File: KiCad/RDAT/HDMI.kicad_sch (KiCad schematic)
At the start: 37 parts, among them J3 HDMI_A, Q4 2N7002, Q5 2SK3018, Q6 2SK3018, Q7 2SK3018, U13 TPAZ1023-04F, U14 TPAZ1023-04F

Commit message: Added Libs and DOCS
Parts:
- J3: footprint A_HDJ_Library:HDMI_A_Molex_208658-1001_Horizontal -> footprints:AMPHENOL_MHDRA111M0; JLCPCB_LINK (none) -> https://www.digikey.com/en/products/detail/amphenol-cs-comm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
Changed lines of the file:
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@@
 			)
 		)
-		(property "Footprint" "A_HDJ_Library:HDMI_A_Molex_208658-1001_Horizontal"
+		(property "Footprint" "footprints:AMPHENOL_MHDRA111M0"
 			(at 179.705 72.39 0)
 			(effects
@@
 			)
 		)
-		(property "Datasheet" "https://en.wikipedia.org/wiki/HDMI"
+		(property "Datasheet" "https://cdn.amphenol-cs.com/media/wysiwyg/files/drawing/mhdra111xx.pdf"
 			(at 179.705 72.39 0)
 			(effects
@@
 			)
 		)
-		(property "JLCPCB_LINK" ""
+		(property "JLCPCB_LINK" "https://www.digikey.com/en/products/detail/amphenol-cs-commercial-products/MHDRA111M0/8572891"
 			(at 179.07 72.39 0)
 			(effects
@@
 					(size 1.27 1.27)
 				)
+				(hide yes)
 			)
 		)

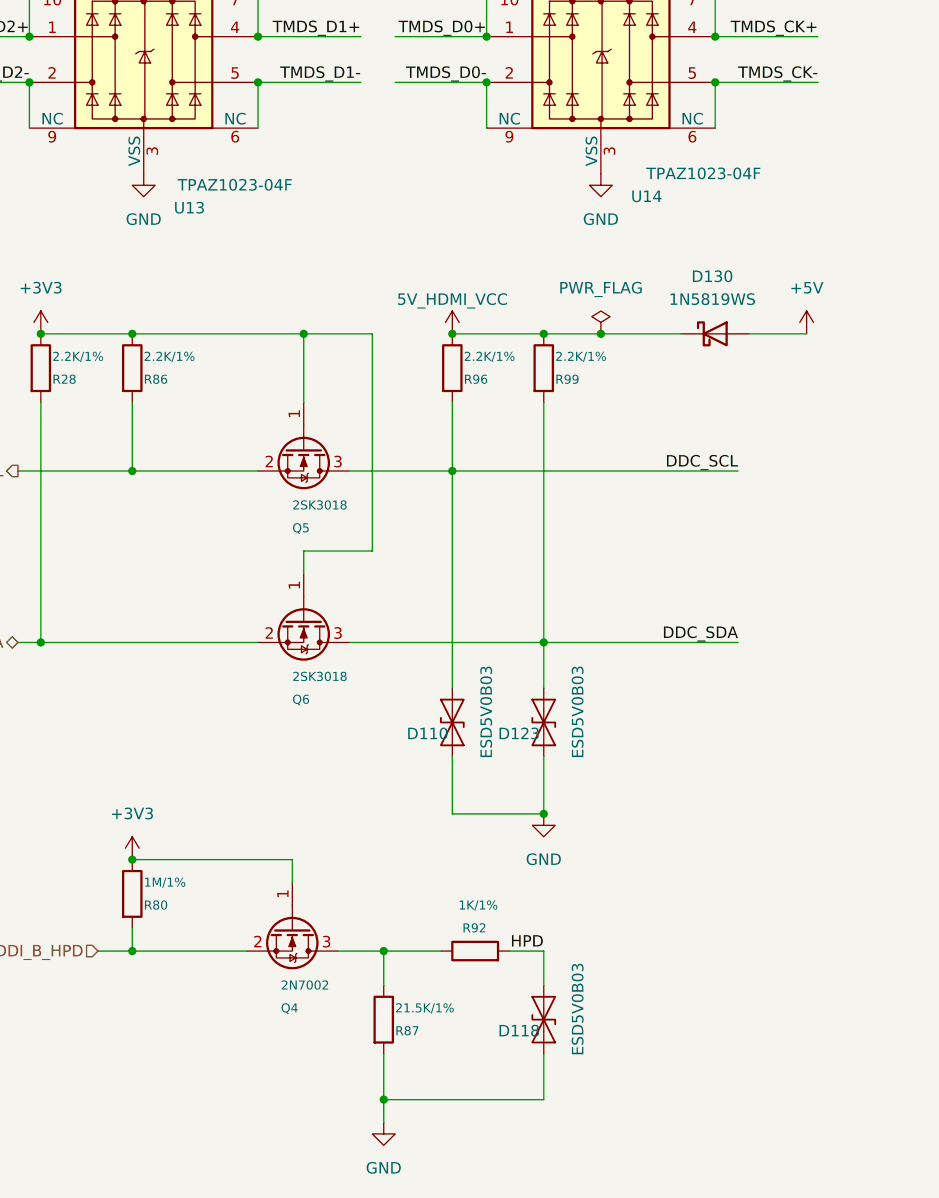
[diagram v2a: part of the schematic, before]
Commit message: Sourced and documented all parts
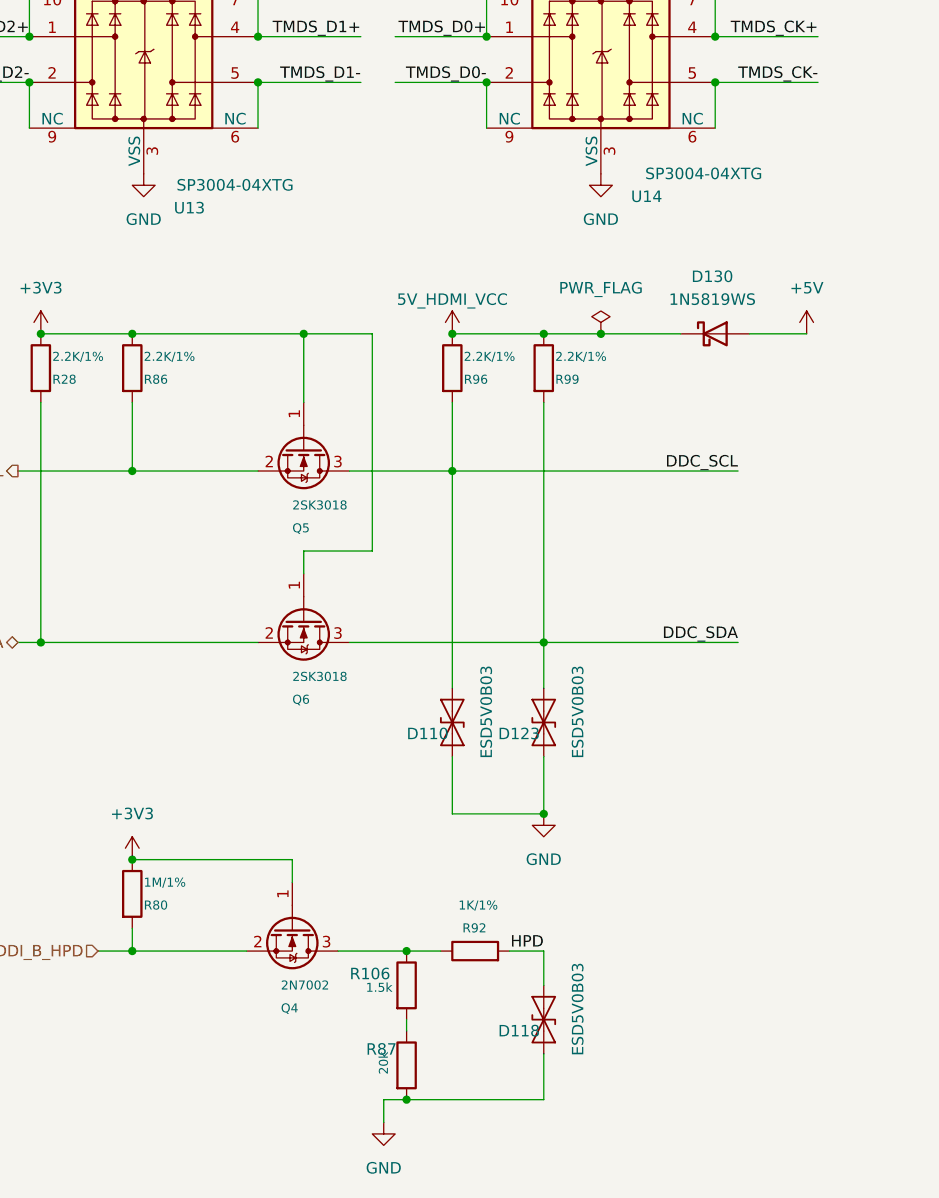
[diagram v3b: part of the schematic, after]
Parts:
- added R106: 1.5k, A_HDJ_Library:R_0402_1005Metric, symbol Device:R
- C25, C26, C27, C28, C29, C30, C31, C91, C92: JLCPCB_LINK (none) -> https://jlcpcb.com/partdetail/291005-CL05B104KB54PNC/C307331
- D110, D118, D123: footprint A_HDJ_Library:D_0402_1005Metric -> Diode_SMD:D_SOD-882; JLCPCB_LINK (none) -> https://jlcpcb.com/partdetail/TechPublic-ESD5V0B031006/C521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
- D130: JLCPCB_LINK (none) -> https://jlcpcb.com/partdetail/GuangdongHottech-1N5819WS/C19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
- F1: JLCPCB_LINK (none) -> https://jlcpcb.com/partdetail/Littelfuse-0805L050WR/C207022
- Q4: JLCPCB_LINK (none) -> https://jlcpcb.com/partdetail/9040-2N7002/C8545
- Q5, Q6, Q7: JLCPCB_LINK (none) -> https://jlcpcb.com/partdetail/GuangdongHottech-2SK3018/C181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
- R100, R28, R86, R96, R99: JLCPCB_LINK (none) -> https://jlcpcb.com/partdetail/26622-0402WGF2201TCE/C25879
- R80: JLCPCB_LINK (none) -> https://jlcpcb.com/partdetail/26826-0402WGF1004TCE/C26083
- R87: value 21.5K/1% -> 20k; JLCPCB_LINK (none) -> https://jlcpcb.com/partdetail/26508-0402WGF2002TCE/C25765
- R88, R89, R90, R91, R93, R95, R97, R98: JLCPCB_LINK (none) -> https://jlcpcb.com/partdetail/TexasInstruments-CSD85302L/C7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
- R92: JLCPCB_LINK (none) -> https://jlcpcb.com/partdetail/12256-0402WGF1001TCE/C11702
- U13, U14: value TPAZ1023-04F -> SP3004-04XTG; footprint A_HDJ_Library:Diodes_UDFN-10_1.0x2.5mm_P0.5mm -> Package_TO_SOT_SMD:SOT-563; JLCPCB_LINK (none) -> https://jlcpcb.com/partdetail/Littelfuse-SP300404XTG/C207280
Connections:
- net at Q4.3 (D), R92.1: now also R106.1; no longer R87.1
- new net: R106.2, R87.1

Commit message: Push before Board Layout
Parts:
- C25, C26, C27, C28, C29, C30, C31, C91, C92: footprint A_HDJ_Library:C_0402_1005Metric -> Capacitor_SMD:C_0402_1005Metric
- D130: footprint A_HDJ_Library:D_SOD-323 -> Diode_SMD:D_SOD-323
- F1: footprint A_HDJ_Library:R_0603_1608Metric -> Fuse:Fuse_0805_2012Metric
- Q4, Q5, Q6, Q7: footprint A_HDJ_Library:SOT-23 -> Package_TO_SOT_SMD:SOT-23
- R100, R106, R28, R80, R86, R87, R88, R89, R90, R91, R92, R93, R95, R96, R97, R98, R99: footprint A_HDJ_Library:R_0402_1005Metric -> Resistor_SMD:R_0402_1005Metric
- renumbered J3 to J6
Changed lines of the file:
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@@
 			)
 		)
-		(property "Footprint" "A_HDJ_Library:R_0402_1005Metric"
+		(property "Footprint" "Resistor_SMD:R_0402_1005Metric"
 			(at 42.672 173.99 90)
 			(effects
@@
 			)
 		)
-		(property "Footprint" "A_HDJ_Library:R_0402_1005Metric"
+		(property "Footprint" "Resistor_SMD:R_0402_1005Metric"
 			(at 42.672 232.41 90)
 			(effects
@@
 			)
 		)
-		(property "Footprint" "A_HDJ_Library:R_0402_1005Metric"
+		(property "Footprint" "Resistor_SMD:R_0402_1005Metric"
 			(at 66.802 64.77 90)
 			(effects
@@
 			)
 		)
-		(property "Footprint" "A_HDJ_Library:C_0402_1005Metric"
+		(property "Footprint" "Capacitor_SMD:C_0402_1005Metric"
 			(at 38.1 37.1348 0)
 			(effects
@@
 			)
 		)
-		(property "Footprint" "A_HDJ_Library:C_0402_1005Metric"
+		(property "Footprint" "Capacitor_SMD:C_0402_1005Metric"
 			(at 38.1 28.2448 0)
 			(effects
@@
 			)
 		)
-		(property "Footprint" "A_HDJ_Library:R_0402_1005Metric"
+		(property "Footprint" "Resistor_SMD:R_0402_1005Metric"
 			(at 78.232 173.99 90)
 			(effects
@@
 			)
 		)
-		(property "Footprint" "A_HDJ_Library:D_SOD-323"
+		(property "Footprint" "Diode_SMD:D_SOD-323"
 			(at 109.22 174.625 0)
 			(effects
@@
 			)
 		)
-		(property "Footprint" "A_HDJ_Library:R_0402_1005Metric"
+		(property "Footprint" "Resistor_SMD:R_0402_1005Metric"
 			(at 82.55 240.538 90)
 			(effects
@@
 			)
 		)
-		(property "Footprint" "A_HDJ_Library:C_0402_1005Metric"
+		(property "Footprint" "Capacitor_SMD:C_0402_1005Metric"
 			(at 38.1 14.2748 0)
 			(effects
@@
 			)
 		)
-		(property "Footprint" "A_HDJ_Library:R_0603_1608Metric"
+		(property "Footprint" "Fuse:Fuse_0805_2012Metric"
 			(at 177.292 36.83 90)
 			(effects
@@
 			)
 		)
-		(property "Footprint" "A_HDJ_Library:C_0402_1005Metric"
+		(property "Footprint" "Capacitor_SMD:C_0402_1005Metric"
 			(at 187.96 30.7848 0)
 			(effects
@@
 		(dnp no)
 		(fields_autoplaced yes)
-		(property "Reference" "J3"
-			(at 190.5 71.12 0)
+		(property "Reference" "J6"
+			(at 190.5 71.1199 0)
 			(effects
 				(font
@@
 		)
 		(property "Value" "HDMI_A"
-			(at 190.5 73.66 0)
+			(at 190.5 73.6599 0)
 			(effects
 				(font
@@
 			(project "RDAT"
 				(path "/0db9370a-8a21-4fd2-83a9-f207c3725dc9/ff947762-4f52-404d-b941-6166ab828992"
-					(reference "J3")
+					(reference "J6")
 					(unit 1)
 				)
@@
 			)
 		)
-		(property "Footprint" "A_HDJ_Library:C_0402_1005Metric"
+		(property "Footprint" "Capacitor_SMD:C_0402_1005Metric"
 			(at 38.1 39.6748 0)
 			(effects
@@
 			)
 		)
-		(property "Footprint" "A_HDJ_Library:R_0402_1005Metric"
+		(property "Footprint" "Resistor_SMD:R_0402_1005Metric"
 			(at 73.152 251.46 90)
 			(effects
@@
 			)
 		)
-		(property "Footprint" "A_HDJ_Library:R_0402_1005Metric"
+		(property "Footprint" "Resistor_SMD:R_0402_1005Metric"
 			(at 64.262 64.77 90)
 			(effects
@@
 			)
 		)
-		(property "Footprint" "A_HDJ_Library:R_0402_1005Metric"
+		(property "Footprint" "Resistor_SMD:R_0402_1005Metric"
 			(at 45.212 64.77 90)
 			(effects
@@
 			)
 		)
-		(property "Footprint" "A_HDJ_Library:R_0402_1005Metric"
+		(property "Footprint" "Resistor_SMD:R_0402_1005Metric"
 			(at 82.55 85.852 90)
 			(effects
@@
 			)
 		)
-		(property "Footprint" "A_HDJ_Library:C_0402_1005Metric"
+		(property "Footprint" "Capacitor_SMD:C_0402_1005Metric"
 			(at 38.1 16.8148 0)
 			(effects
@@
 			)
 		)
-		(property "Footprint" "A_HDJ_Library:SOT-23"
+		(property "Footprint" "Package_TO_SOT_SMD:SOT-23"
 			(at 61.595 207.01 0)
 			(effects
@@
 			)
 		)
-		(property "Footprint" "A_HDJ_Library:R_0402_1005Metric"
+		(property "Footprint" "Resistor_SMD:R_0402_1005Metric"
 			(at 57.912 64.77 90)
 			(effects
@@
 			)
 		)
-		(property "Footprint" "A_HDJ_Library:R_0402_1005Metric"
+		(property "Footprint" "Resistor_SMD:R_0402_1005Metric"
 			(at 51.562 64.77 90)
 			(effects
@@
 			)
 		)
-		(property "Footprint" "A_HDJ_Library:SOT-23"
+		(property "Footprint" "Package_TO_SOT_SMD:SOT-23"
 			(at 60.325 241.3 0)
 			(effects
@@
 			)
 		)
-		(property "Footprint" "A_HDJ_Library:C_0402_1005Metric"
+		(property "Footprint" "Capacitor_SMD:C_0402_1005Metric"
 			(at 38.1 25.7048 0)
 			(effects
@@
 			)
 		)
-		(property "Footprint" "A_HDJ_Library:SOT-23"
+		(property "Footprint" "Package_TO_SOT_SMD:SOT-23"
 			(at 66.04 89.535 0)
 			(effects
@@
 			)
 		)
-		(property "Footprint" "A_HDJ_Library:R_0402_1005Metric"
+		(property "Footprint" "Resistor_SMD:R_0402_1005Metric"
 			(at 73.152 242.57 90)
 			(effects
@@
 			)
 		)
-		(property "Footprint" "A_HDJ_Library:R_0402_1005Metric"
+		(property "Footprint" "Resistor_SMD:R_0402_1005Metric"
 			(at 88.392 173.99 90)
 			(effects
@@
 			)
 		)
-		(property "Footprint" "A_HDJ_Library:R_0402_1005Metric"
+		(property "Footprint" "Resistor_SMD:R_0402_1005Metric"
 			(at 32.512 173.99 90)
 			(effects
@@
 			)
 		)
-		(property "Footprint" "A_HDJ_Library:C_0402_1005Metric"
+		(property "Footprint" "Capacitor_SMD:C_0402_1005Metric"
 			(at 38.1 51.1048 0)
 			(effects
@@
 			)
 		)
-		(property "Footprint" "A_HDJ_Library:R_0402_1005Metric"
+		(property "Footprint" "Resistor_SMD:R_0402_1005Metric"
 			(at 54.102 64.77 90)
 			(effects
@@
 			)
 		)
-		(property "Footprint" "A_HDJ_Library:C_0402_1005Metric"
+		(property "Footprint" "Capacitor_SMD:C_0402_1005Metric"
 			(at 38.1 48.5648 0)
 			(effects
@@
 			)
 		)
-		(property "Footprint" "A_HDJ_Library:SOT-23"
+		(property "Footprint" "Package_TO_SOT_SMD:SOT-23"
 			(at 61.595 187.96 0)
 			(effects
@@
 			)
 		)
-		(property "Footprint" "A_HDJ_Library:R_0402_1005Metric"
+		(property "Footprint" "Resistor_SMD:R_0402_1005Metric"
 			(at 47.752 64.77 90)
 			(effects
@@
 			)
 		)
-		(property "Footprint" "A_HDJ_Library:R_0402_1005Metric"
+		(property "Footprint" "Resistor_SMD:R_0402_1005Metric"
 			(at 60.452 64.77 90)
 			(effects

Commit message: End Of day commit
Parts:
- removed U13, U14: SP3004-04XTG, Package_TO_SOT_SMD:SOT-563, symbol Power_Protection:D3V3XA4B10LP
- added D104, D107, D108, D115: PESD2USB3UV-TR, Package_TO_SOT_SMD:SOT-23, symbol Power_Protection_Mod:RCLAMP0502BA
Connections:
- net GND: now also J6.SH1 (SH), J6.SH2 (SH), D104.3 (A), D107.3 (A), D108.3 (A), D115.3 (A); no longer J6.SH
- net TMDS_CK+: now also D115.1 (K1)
- net TMDS_CK-: now also D115.2 (K2)
- net TMDS_D0+: now also D108.1 (K1)
- net TMDS_D0-: now also D108.2 (K2)
- net TMDS_D1+: now also D104.1 (K1)
- net TMDS_D1-: now also D104.2 (K2)
- net TMDS_D2+: now also D107.1 (K1)
- net TMDS_D2-: now also D107.2 (K2)

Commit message: 2x checing of bom on JLCPCB
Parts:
- C25, C26, C27, C28, C29, C30, C31, C91, C92: value 100nF/50V -> 100nF
- R100, R28, R86, R96, R99: value 2.2K/1% -> 2.2K
- R80: value 1M/1% -> 1M; JLCPCB_PART_NUMBER (none) -> C26083
- R88, R89, R90, R91, R93, R95, R97, R98: value 470R/1% -> 470R; JLCPCB_LINK https://jlcpcb.com/partdetail/TexasInstruments-CSD85302L/C7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 -> https://jlcpcb.com/partdetail/26487-0402WGF1002TCE/C25744; JLCPCB_PART_NUMBER (none) -> C25744
- R92: value 1K/1% -> 1K

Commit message: Generate Gerbers and Order PCB
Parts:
- R88: JLCPCB_LINK https://jlcpcb.com/partdetail/26487-0402WGF1002TCE/C25744 -> https://jlcpcb.com/partdetail/25860-0402WGF4700TCE/C25117
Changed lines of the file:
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@@
 			)
 		)
-		(property "JLCPCB_LINK" "https://jlcpcb.com/partdetail/26487-0402WGF1002TCE/C25744"
+		(property "JLCPCB_LINK" "https://jlcpcb.com/partdetail/25860-0402WGF4700TCE/C25117"
 			(at 46.99 64.77 0)
 			(effects
